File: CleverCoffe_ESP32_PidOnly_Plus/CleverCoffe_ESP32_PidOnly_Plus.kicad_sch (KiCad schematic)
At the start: 17 parts

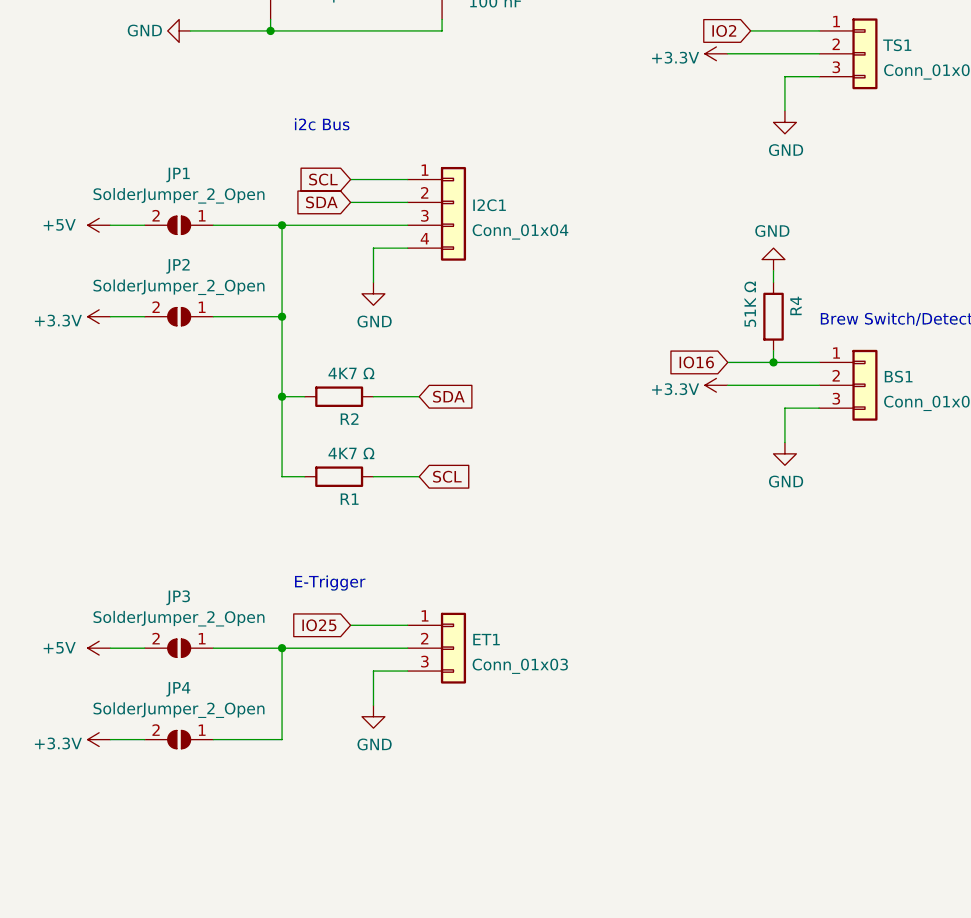
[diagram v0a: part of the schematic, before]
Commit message: User 3-pole solder jumpers for voltage selection
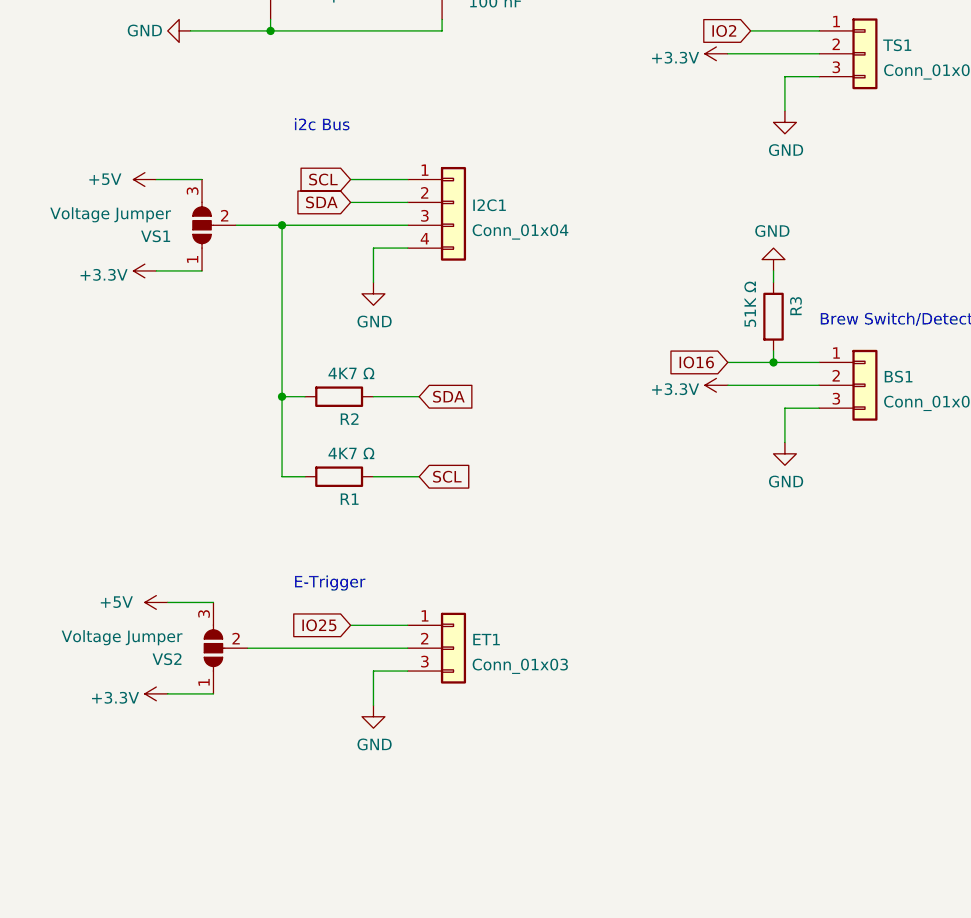
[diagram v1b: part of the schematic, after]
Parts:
- removed JP1, JP2, JP3, JP4: SolderJumper_2_Open, Jumper:SolderJumper-2_P1.3mm_Open_Pad1.0x1.5mm, symbol Jumper:SolderJumper_2_Open
- added VS1, VS2: Voltage Jumper, Jumper:SolderJumper-3_P1.3mm_Open_Pad1.0x1.5mm_NumberLabels, symbol Jumper:SolderJumper_3_Open
- renumbered R4 to R3
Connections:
- net +3V3: now also VS1.1 (A), VS2.1 (A)
- net +5V: now also VS1.3 (B), VS2.3 (B)
- net at I2C1.3 (Pin_3), R1.2, R2.2: now also VS1.2 (C)
- net at ET1.2 (Pin_2): now also VS2.2 (C)
